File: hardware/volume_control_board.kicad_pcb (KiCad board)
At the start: 2 copper layers, 75.7 x 47.6 mm, 43 parts, among them J1 Screw_Terminal_01x08, J2 AudioJack3, J3 Conn_01x04, J4 Conn_01x04, J5 Conn_01x04, J6 RXTX/CAN, SW1 Rotary_Encoder_Switch, U1 Teensy3.2, U2 AD5254

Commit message: firmware v1 and board v2
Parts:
- added J10: Conn_01x03, Socket_Strips:Socket_Strip_Straight_1x03_Pitch2.00mm, F.Cu at (133.7, 78.8)
- added J7: Conn_01x04, Connectors:Grove_1x04, F.Cu at (142.1, 87.8)
- added J8: Conn_01x03, Socket_Strips:Socket_Strip_Straight_1x03_Pitch2.00mm, F.Cu at (133.6, 67.6)
- added J9: Conn_01x03, Socket_Strips:Socket_Strip_Straight_1x03_Pitch2.00mm, F.Cu at (126.7, 73.9)
- J3: footprint Socket_Strips:Socket_Strip_Straight_1x04_Pitch2.54mm -> Connectors:Grove_1x04
- J4: value Conn_01x04 -> 5V in; footprint Socket_Strips:Socket_Strip_Straight_1x04_Pitch2.54mm -> Socket_Strips:Socket_Strip_Straight_1x02_Pitch2.54mm
- J5: value Conn_01x04 -> Conn_01x03; footprint Socket_Strips:Socket_Strip_Straight_1x04_Pitch2.54mm -> Socket_Strips:Socket_Strip_Straight_1x03_Pitch2.00mm
- moved J4 28.5 mm to (109.0, 56.4), turned to 90 degrees
- moved SW1 14.5 mm to (155.2, 84.6), turned to 270 degrees
- moved R12 7.63 mm to (109.0, 61.6), turned to 90 degrees
- moved J3 7.52 mm to (136.3, 87.8), turned to 0 degrees
- moved R10 7.30 mm to (118.2, 79.8), turned to 270 degrees
- moved R3 6.44 mm to (114.3, 79.8)
- moved R13 6.23 mm to (106.9, 61.6), turned to 90 degrees
- moved R11 5.42 mm to (116.3, 79.8), turned to 270 degrees
- moved J2 4.85 mm to (154.6, 71.8)
- moved C1 4.03 mm to (111.0, 61.6), turned to 90 degrees
- moved J5 3.31 mm to (126.7, 63.5)
- moved REF** 2.41 mm to (81.5, 56.6)
- moved REF** 2.41 mm to (81.5, 99.4)
- moved J6 2.03 mm to (82.7, 69.2)
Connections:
- J3 pad 1: Net-(J3-Pad1) -> GND
- J3 pad 4: GND -> Net-(J3-Pad4)
- J4 pad 1: Net-(J4-Pad1) -> +5V
- J4 pad 2: LEFT_IN -> GND
- J5 pad 1: FRONT_L_OUT -> LEFT_IN
- J5 pad 2: REAR_L_OUT -> FRONT_L_OUT
- J5 pad 3: FRONT_R_OUT -> GNDA
- R4 pad 2: Net-(J3-Pad1) -> Net-(J3-Pad4)
- R5 pad 1: Net-(J3-Pad2) -> Net-(J3-Pad3)
- R6 pad 2: Net-(J3-Pad1) -> Net-(J3-Pad4)
- R7 pad 2: Net-(J3-Pad2) -> Net-(J3-Pad3)
- R8 pad 2: Net-(J3-Pad3) -> Net-(J3-Pad2)
- R9 pad 2: Net-(J3-Pad3) -> Net-(J3-Pad2)
- SW1 pad A: Net-(J3-Pad1) -> Net-(J3-Pad4)
- SW1 pad B: Net-(J3-Pad2) -> Net-(J3-Pad3)
- SW1 pad S1: Net-(J3-Pad3) -> Net-(J3-Pad2)
- U1 pad 31: Net-(U1-Pad31) -> +3V3
- U2 pad 1: Net-(J4-Pad1) -> FRONT_L_OUT
- U2 pad 11: FRONT_R_OUT -> RIGHT_IN
- U2 pad 12: Net-(J4-Pad3) -> GNDA
- U2 pad 13: Net-(J4-Pad3) -> FRONT_R_OUT
- U2 pad 17: REAR_R_OUT -> RIGHT_IN
- U2 pad 18: RIGHT_IN -> GNDA
- U2 pad 19: RIGHT_IN -> REAR_R_OUT
- U2 pad 2: Net-(J4-Pad1) -> GNDA
- U2 pad 3: FRONT_L_OUT -> LEFT_IN
- U2 pad 6: LEFT_IN -> REAR_L_OUT
- U2 pad 7: LEFT_IN -> GNDA
- U2 pad 8: REAR_L_OUT -> LEFT_IN
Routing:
- net GNDA: track 45.1 -> 193.2 mm, vias 0 -> 4
- net Net-(J3-Pad4): track 0.00 -> 51.2 mm
- net Net-(J3-Pad1): track 42.3 -> 0.00 mm
- net RIGHT_IN: track 53.9 -> 93.4 mm
- net Net-(J4-Pad3): track 36.0 -> 0.00 mm, vias 2 -> 0
- net Net-(J3-Pad2): track 12.6 -> 33.4 mm, vias 0 -> 1
- net REAR_R_OUT: track 48.6 -> 65.2 mm
- net LEFT_IN: track 35.9 -> 50.2 mm, vias 1 -> 2
- net Net-(J4-Pad1): track 13.8 -> 0.00 mm
- net GND: track 38.0 -> 51.2 mm, vias 8 -> 7
- net Net-(J3-Pad3): track 38.1 -> 25.2 mm
- net FRONT_R_OUT: track 43.3 -> 55.7 mm
- net Net-(C1-Pad1): track 3.87 -> 11.9 mm
- net Net-(R12-Pad1): track 5.21 -> 12.6 mm
- net FRONT_L_OUT: track 29.1 -> 22.4 mm
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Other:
- board size 75.7 x 47.6 mm -> 81.5 x 47.6 mm
- board text added: "A0 W0 B0"
- board text added: "A1 W1 B1"
- board text added: "A2 W2 B2"
- board text added: "A3 W3 B3"
- board text added: "CH1 CH2 CH3 CH4"
- board text removed: "Ch 1 in Ch 2 in Ch 3 in Ch 4 in"
- board text removed: "Ch 1 out Ch 2 out Ch 3 out Ch 4 out"

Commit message: added a few resistors for adjusting later.
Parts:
- added R14: 10K, Resistors_SMD:R_0805, F.Cu at (140.3, 64.5)
- added R15: 10K, Resistors_SMD:R_0805, F.Cu at (140.3, 66.7)
- added R16: 10K, Resistors_SMD:R_0805, F.Cu at (140.3, 73.3)
- added R17: 10K, Resistors_SMD:R_0805, F.Cu at (140.3, 75.4)
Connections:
- J10 pad 1: RIGHT_IN -> Net-(J10-Pad1)
- J5 pad 1: LEFT_IN -> Net-(J5-Pad1)
- J8 pad 1: LEFT_IN -> Net-(J8-Pad1)
- J9 pad 1: RIGHT_IN -> Net-(J9-Pad1)
- U2 pad 11: RIGHT_IN -> Net-(J9-Pad1)
- U2 pad 17: RIGHT_IN -> Net-(J10-Pad1)
- U2 pad 3: LEFT_IN -> Net-(J5-Pad1)
- U2 pad 8: LEFT_IN -> Net-(J8-Pad1)
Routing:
- net RIGHT_IN: track 93.4 -> 20.0 mm, vias 2 -> 0
- net Net-(J10-Pad1): track 0.00 -> 43.1 mm, vias 0 -> 1
- net Net-(J9-Pad1): track 0.00 -> 37.9 mm, vias 0 -> 1
- net LEFT_IN: track 50.2 -> 13.3 mm, vias 2 -> 0
- net Net-(J8-Pad1): track 0.00 -> 23.2 mm, vias 0 -> 1
- net Net-(J5-Pad1): track 0.00 -> 22.4 mm, vias 0 -> 1

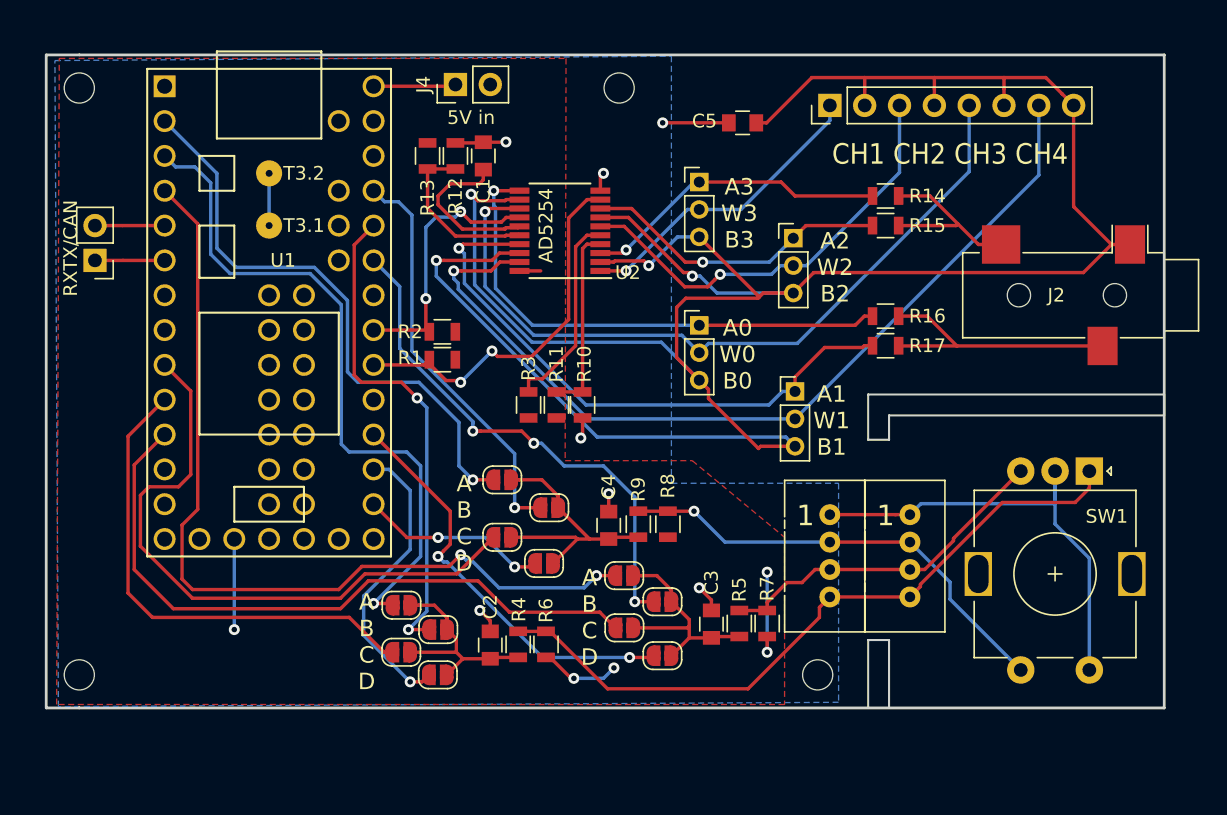
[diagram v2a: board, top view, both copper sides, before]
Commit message: updated board with more breakouts.
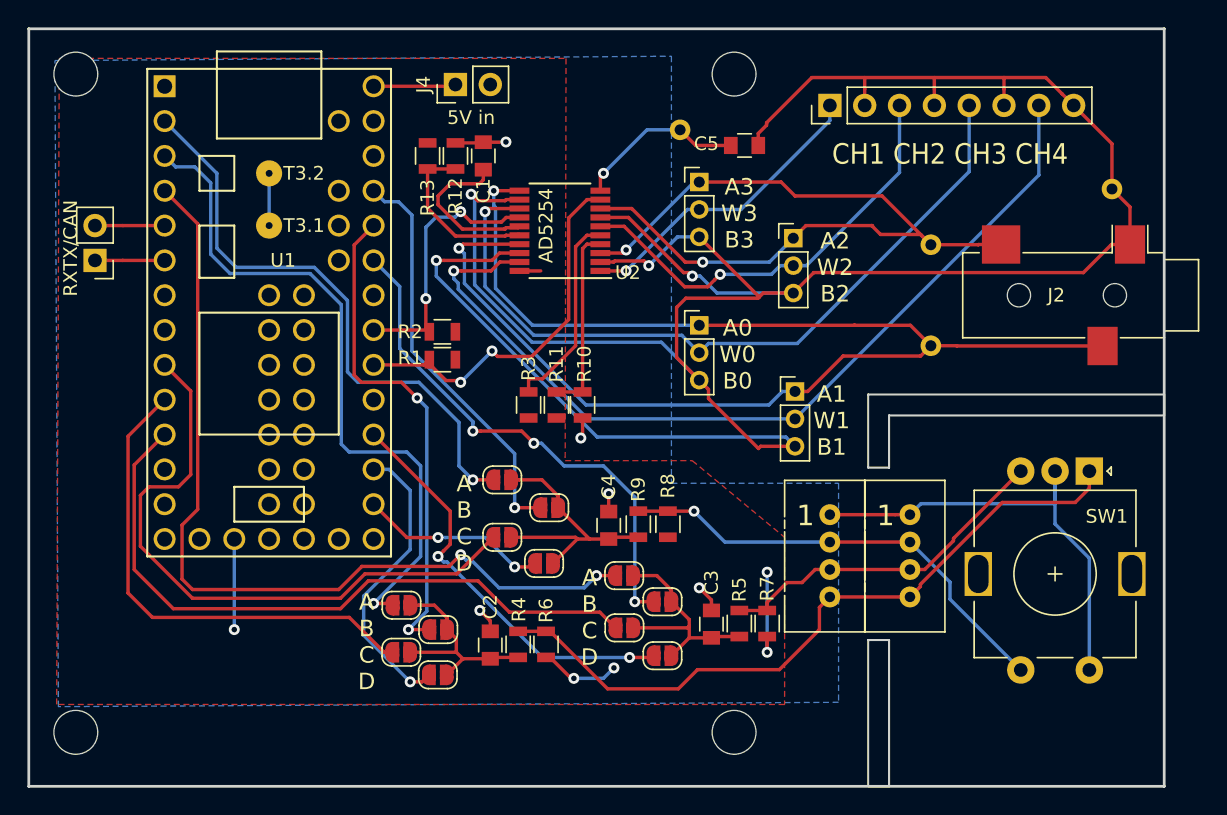
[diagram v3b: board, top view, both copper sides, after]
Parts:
- removed R14, R15, R16, R17: 10K, Resistors_SMD:R_0805
- added TP1: TestPoint, Measurement_Points:Measurement_Point_Round-TH_Small, F.Cu at (143.6, 75.4)
- added TP2: TestPoint, Measurement_Points:Measurement_Point_Round-TH_Small, F.Cu at (143.6, 68.1)
- added TP3: TestPoint, Measurement_Points:Measurement_Point_Round-TH_Small, F.Cu at (125.3, 59.7)
- added TP4: TestPoint, Measurement_Points:Measurement_Point_Round-TH_Small, F.Cu at (156.8, 64.0)
- REF** (x4): value MountingHole_2.2mm_M2 -> MountingHole_3.2mm_M3; footprint Mounting_Holes:MountingHole_2.2mm_M2 -> Mounting_Holes:MountingHole_3.2mm_M3
- moved REF** 8.44 mm to (129.3, 55.6)
- moved REF** 7.40 mm to (129.3, 103.6)
- moved REF** 4.20 mm to (81.3, 103.6)
- moved C5 1.66 mm to (130.0, 60.8)
- moved REF** 1.05 mm to (81.3, 55.6)
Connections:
- J10 pad 1: Net-(J10-Pad1) -> RIGHT_IN
- J5 pad 1: Net-(J5-Pad1) -> LEFT_IN
- J8 pad 1: Net-(J8-Pad1) -> LEFT_IN
- J9 pad 1: Net-(J9-Pad1) -> RIGHT_IN
- U2 pad 11: Net-(J9-Pad1) -> RIGHT_IN
- U2 pad 17: Net-(J10-Pad1) -> RIGHT_IN
- U2 pad 3: Net-(J5-Pad1) -> LEFT_IN
- U2 pad 8: Net-(J8-Pad1) -> LEFT_IN
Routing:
- net RIGHT_IN: track 20.0 -> 101.9 mm, vias 0 -> 2
- net LEFT_IN: track 13.3 -> 61.4 mm, vias 0 -> 2
- net Net-(J10-Pad1): track 43.1 -> 0.00 mm, vias 1 -> 0
- net Net-(J9-Pad1): track 37.9 -> 0.00 mm, vias 1 -> 0
- net Net-(J8-Pad1): track 23.2 -> 0.00 mm, vias 1 -> 0
- net Net-(J5-Pad1): track 22.4 -> 0.00 mm, vias 1 -> 0
- net GND: track 51.2 -> 57.6 mm, vias 7 -> 6
- net GNDA: track 193.2 -> 195.0 mm
- net Net-(J3-Pad4): track 51.2 -> 51.7 mm
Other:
- board size 81.5 x 47.6 mm -> 82.8 x 55.2 mm

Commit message: added silk pin descriptions.
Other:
- board text added: "A_ENCA"
- board text added: "A_ENCB"
- board text added: "A_PUSH"
- board text added: "B_ENCA"
- board text added: "B_ENCB"
- board text added: "B_PUSH"
- board text added: "C_ENCA"
- board text added: "C_ENCB"
- board text added: "C_PUSH"
- board text added: "D_ENCA"
- board text added: "D_ENCB"
- board text added: "D_PUSH"
- board text added: "GND Push Switch Encoder B Encoder A"
- board text added: "SCL"
- board text added: "SDA"
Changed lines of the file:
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@@
   (general
     (thickness 1.6)
-    (drawings 23)
+    (drawings 38)
     (tracks 494)
     (zones 0)
@@
       (net 6 GNDA))
   )
+  (gr_text "GND\nPush Switch\nEncoder B\nEncoder A" (at 134.874 90.805) (layer B.SilkS)
+    (effects (font (size 1.2 1.2) (thickness 0.25)) (justify left mirror))
+  )
+  (gr_text SCL (at 106.045 74.422) (layer B.SilkS)
+    (effects (font (size 1.2 1.2) (thickness 0.25)) (justify mirror))
+  )
+  (gr_text SDA (at 105.918 76.962) (layer B.SilkS)
+    (effects (font (size 1.2 1.2) (thickness 0.25)) (justify mirror))
+  )
+  (gr_text D_ENCB (at 107.442 82.042) (layer B.SilkS)
+    (effects (font (size 1.2 1.2) (thickness 0.25)) (justify mirror))
+  )
+  (gr_text D_ENCA (at 107.569 84.328) (layer B.SilkS)
+    (effects (font (size 1.2 1.2) (thickness 0.25)) (justify mirror))
+  )
+  (gr_text B_ENCB (at 107.315 69.215) (layer B.SilkS)
+    (effects (font (size 1.2 1.2) (thickness 0.25)) (justify mirror))
+  )
+  (gr_text B_ENCA (at 107.442 66.675) (layer B.SilkS)
+    (effects (font (size 1.2 1.2) (thickness 0.25)) (justify mirror))
+  )
+  (gr_text A_ENCA (at 83.312 61.595) (layer B.SilkS)
+    (effects (font (size 1.2 1.2) (thickness 0.25)) (justify mirror))
+  )
+  (gr_text A_ENCB (at 83.185 64.135) (layer B.SilkS)
+    (effects (font (size 1.2 1.2) (thickness 0.25)) (justify mirror))
+  )
+  (gr_text C_ENCB (at 83.185 82.042) (layer B.SilkS)
+    (effects (font (size 1.2 1.2) (thickness 0.25)) (justify mirror))
+  )
+  (gr_text C_ENCA (at 83.185 79.502) (layer B.SilkS)
+    (effects (font (size 1.2 1.2) (thickness 0.25)) (justify mirror))
+  )
+  (gr_text B_PUSH (at 107.569 64.262) (layer B.SilkS)
+    (effects (font (size 1.2 1.2) (thickness 0.25)) (justify mirror))
+  )
+  (gr_text A_PUSH (at 83.185 59.055) (layer B.SilkS)
+    (effects (font (size 1.2 1.2) (thickness 0.25)) (justify mirror))
+  )
+  (gr_text C_PUSH (at 82.931 76.835) (layer B.SilkS)
+    (effects (font (size 1.2 1.2) (thickness 0.25)) (justify mirror))
+  )
+  (gr_text D_PUSH (at 107.569 87.122) (layer B.SilkS)
+    (effects (font (size 1.2 1.2) (thickness 0.25)) (justify mirror))
+  )
   (gr_text "A1\nW1\nB1" (at 136.398 80.899) (layer F.SilkS)
     (effects (font (size 1.2 1.2) (thickness 0.3)))
@@
   (gr_line (start 77.851 107.569) (end 77.851 52.324) (layer Edge.Cuts) (width 0.2))
   (gr_line (start 160.655 107.569) (end 77.851 107.569) (layer Edge.Cuts) (width 0.2))
-  (gr_text "@jus341\n4 channel Digital Potentiometer" (at 126.365 96.393) (layer B.SilkS)
+  (gr_text "@jus341\n4 channel Digital Potentiometer" (at 123.444 103.759) (layer B.SilkS)
     (effects (font (size 1.5 1.5) (thickness 0.3)) (justify left mirror))
   )
